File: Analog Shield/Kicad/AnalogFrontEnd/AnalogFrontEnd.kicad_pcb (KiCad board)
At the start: 4 copper layers, 64.8 x 59.3 mm, 120 parts, among them J1 Digital1, J2 Digital2, J3 Power, J4 Analog1, J5 Analog2, J6 Interface, U1 AD8130ARMZ-REEL7, U10 SN74AHCT1G32DCKR, U11 ADG509FBRUZ, U12 ADG509FBRUZ, U13 AD823AARMZ, U14 SN74HC139DBR, U15 ADG411BRUZ, U16 SN74LVC1G08DBVR, U17 AD8130ARMZ-REEL7, U18 ADG1236YRUZ, U19 ADG1236YRUZ, U2 AD8130ARMZ-REEL7, U20 AD8130ARMZ-REEL7, U21 SN74AHCT1G04DCKR, U22 SN74AHCT1G32DCKR, U23 ADG509FBRUZ, U24 ADG509FBRUZ, U25 AD823AARMZ, U26 ADG411BRUZ, U27 SN74LVC1G08DBVR, U3 AD8130ARMZ-REEL7, U4 AD8130ARMZ-REEL7, U5 AD8130ARMZ-REEL7, U6 ADG1236YRUZ, U7 ADG1236YRUZ, U8 AD8130ARMZ-REEL7, U9 SN74AHCT1G04DCKR

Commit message: Adding B.Cu as a GND plane
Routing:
- added copper zone on B.Cu, net GND
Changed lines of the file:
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@@
     (fp_arc (start 0.799455 1.399868) (mid 0.776917 1.452892) (end 0.723713 1.475) (layer "F.Fab") (width 0.127))
     (fp_arc (start -0.80074 -1.37084) (mid -0.778218 -1.423887) (end -0.724999 -1.445998) (layer "F.Fab") (width 0.127))
-    (fp_arc (start 0.723714 -1.445998) (mid 0.776937 -1.423889) (end 0.799455 -1.37084) (layer "F.Fab") (width 0.127))
+    (fp_arc (start 0.723714 -1.445998) (mid 0.77694 -1.423891) (end 0.799455 -1.37084) (layer "F.Fab") (width 0.127))
     (fp_arc (start -0.724999 1.475) (mid -0.778213 1.452901) (end -0.80074 1.399867) (layer "F.Fab") (width 0.127))
     (pad "1" smd rect (at -1.275001 -0.950001 180) (size 0.549999 0.800001) (layers "F.Cu" "F.Paste" "F.Mask")
@@
     (fp_arc (start -0.80074 -1.37084) (mid -0.778218 -1.423887) (end -0.724999 -1.445998) (layer "F.Fab") (width 0.127))
     (fp_arc (start -0.724999 1.475) (mid -0.778213 1.452901) (end -0.80074 1.399867) (layer "F.Fab") (width 0.127))
-    (fp_arc (start 0.723714 -1.445998) (mid 0.776937 -1.423889) (end 0.799455 -1.37084) (layer "F.Fab") (width 0.127))
+    (fp_arc (start 0.723714 -1.445998) (mid 0.77694 -1.423891) (end 0.799455 -1.37084) (layer "F.Fab") (width 0.127))
     (fp_arc (start 0.799455 1.399868) (mid 0.776917 1.452892) (end 0.723713 1.475) (layer "F.Fab") (width 0.127))
     (pad "1" smd rect (at -1.275001 -0.950001 90) (size 0.549999 0.800001) (layers "F.Cu" "F.Paste" "F.Mask")
@@
   (segment (start 155.5956 90.978) (end 156.149401 91.531801) (width 0.2) (layer "F.Cu") (net 126))
   (segment (start 155.236517 90.3732) (end 155.5956 90.732283) (width 0.2) (layer "F.Cu") (net 126))
-  (zone (net 1) (net_name "GND") (layer "In1.Cu") (hatch edge 0.508)
+  (zone (net 1) (net_name "GND") (layers "In1.Cu" "B.Cu") (hatch edge 0.508)
     (connect_pads (clearance 0.508))
     (min_thickness 0.254) (filled_areas_thickness no)
@@
     (polygon
       (pts
-        (xy 203.7588 106.9848)
-        (xy 113.8428 105.4608)
-        (xy 120.2436 43.2816)
-        (xy 120.396 43.434)
-        (xy 195.3768 42.9768)
+        (xy 200.406 108.0516)
+        (xy 125.1204 107.8992)
+        (xy 124.6632 42.5196)
+        (xy 200.2536 42.5196)
       )
     )

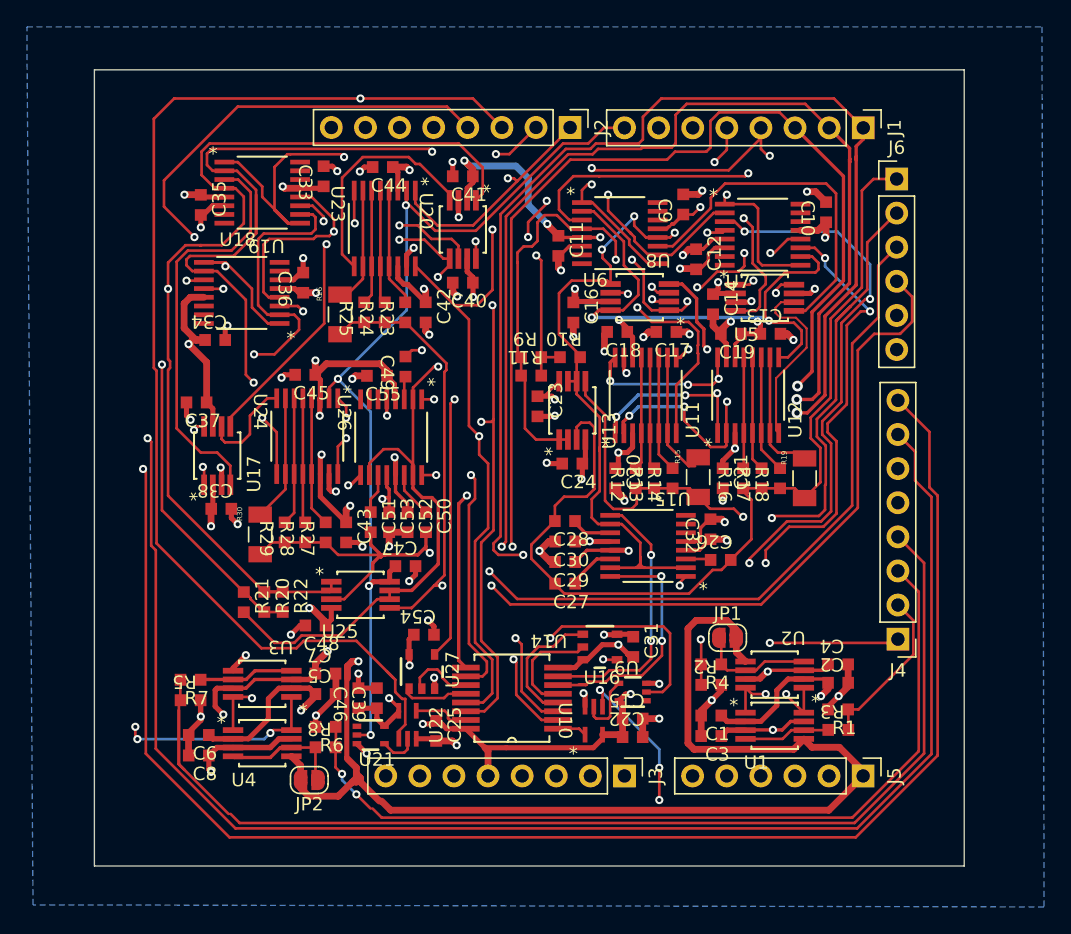
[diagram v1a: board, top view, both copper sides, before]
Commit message: Correcting Trace Errors in Layout Draft
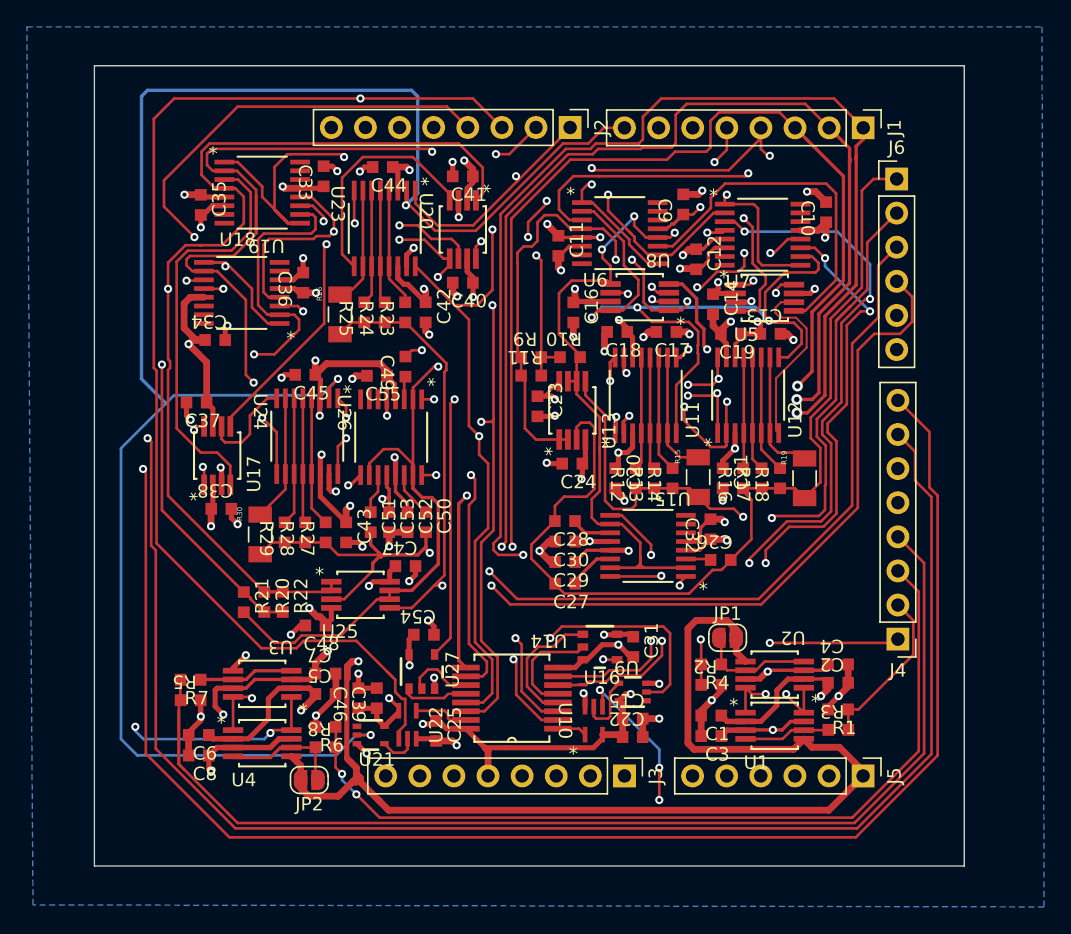
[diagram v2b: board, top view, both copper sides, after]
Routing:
- net /D7: track 67.6 -> 137.8 mm
- net -12V: track 267.7 -> 288.3 mm
- net /Channel 1/S1_01: track 9.90 -> 12.4 mm
- net Net-(U12-Pad9): track 40.7 -> 41.3 mm
- net /CH2_VDM+: track 64.0 -> 63.7 mm, vias 4 -> 3
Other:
- board size 64.8 x 59.3 mm -> 64.8 x 59.6 mm
